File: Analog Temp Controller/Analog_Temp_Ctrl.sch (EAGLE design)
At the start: 110 parts, among them IC1 TL074D, IC3 LMV358MMX, IC4 ADA4522-2, J1 USB_MINI-B_SMT, Q1 TIP41C, T1 2N3904, T2 2N3906, U1 ADR01BRZ, U2 ATMEGA32U4-AU, U3 CJT1117-3.3-SOT223, U4 CJT1117-5.0-SOT223, U5 AD5272BRMZ-20, X1 CRYSTAL-3.2-2.5

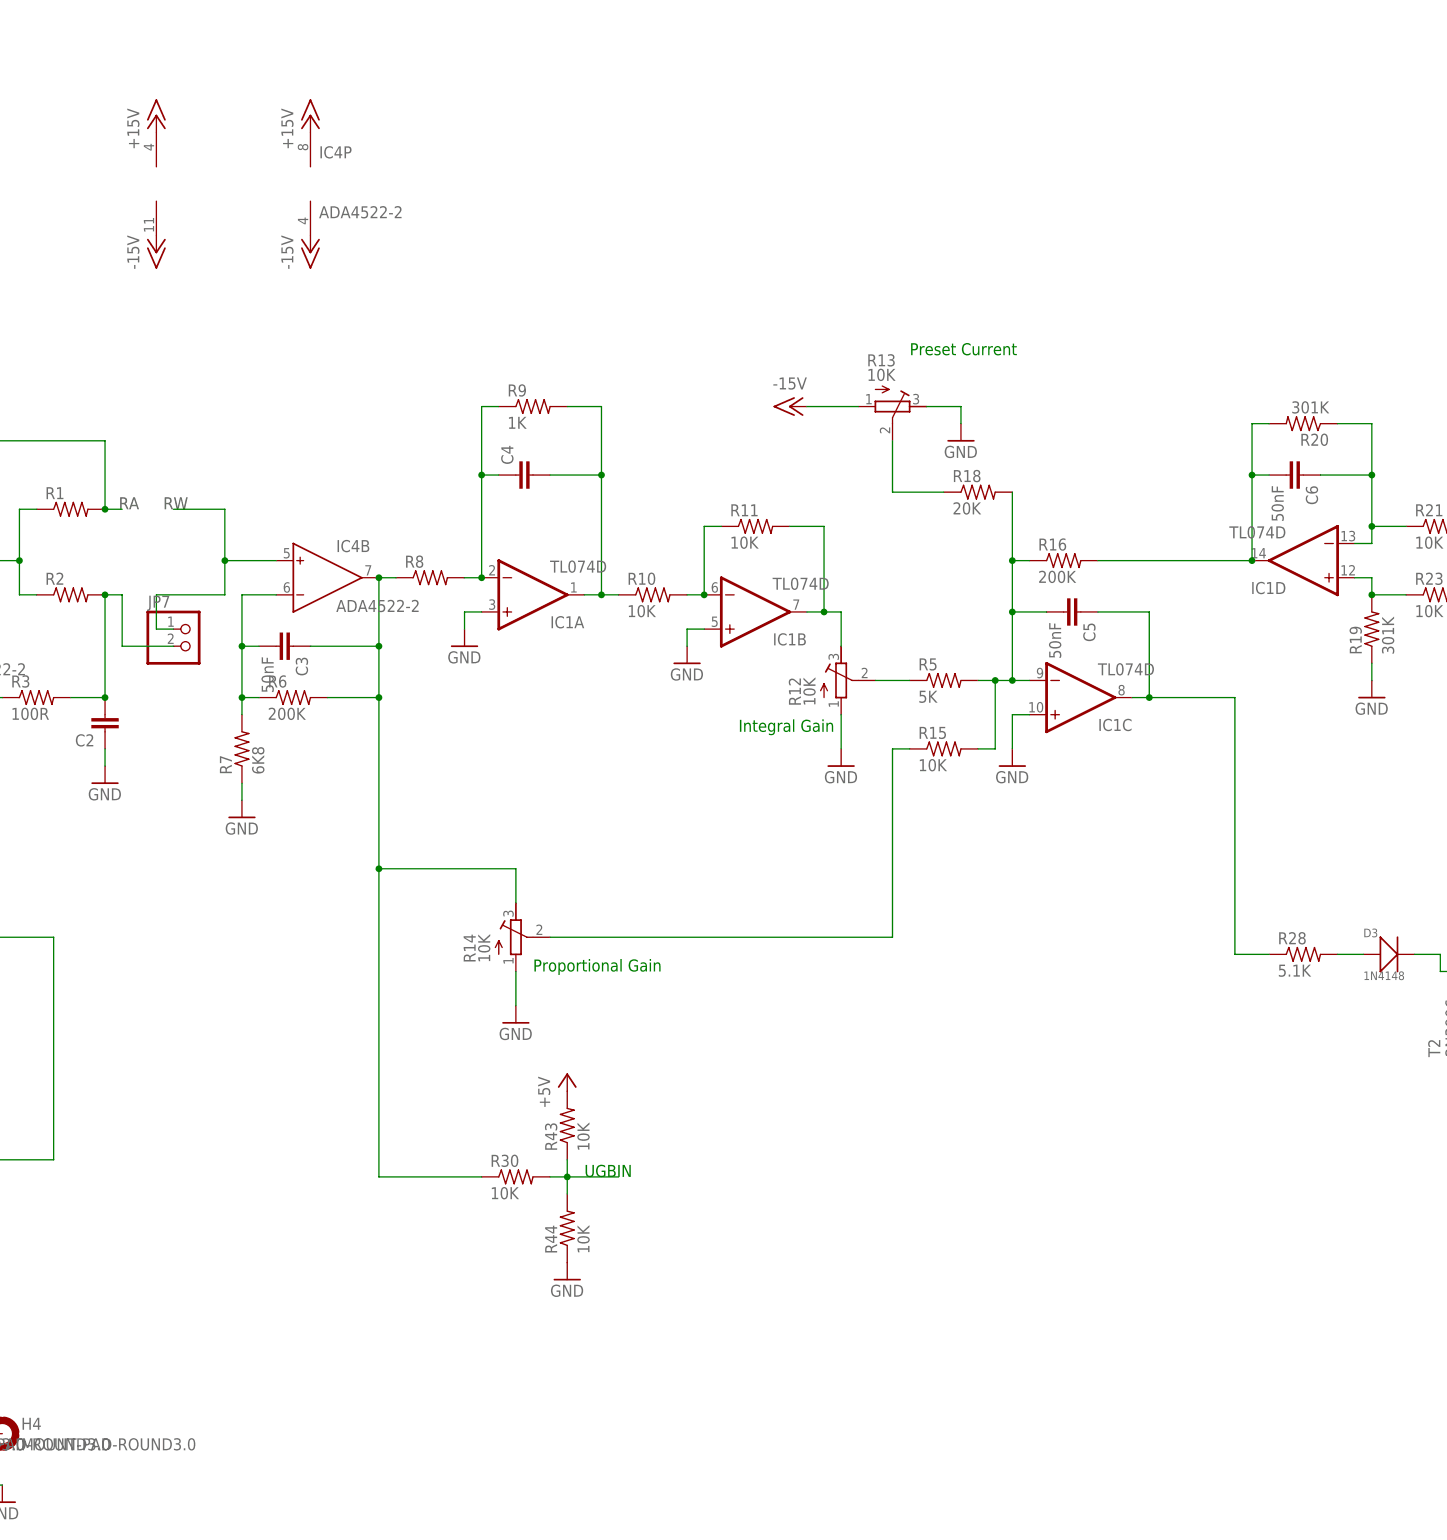
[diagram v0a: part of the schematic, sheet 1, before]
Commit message: Completed Temperature Controller, Rdy for Mfg.
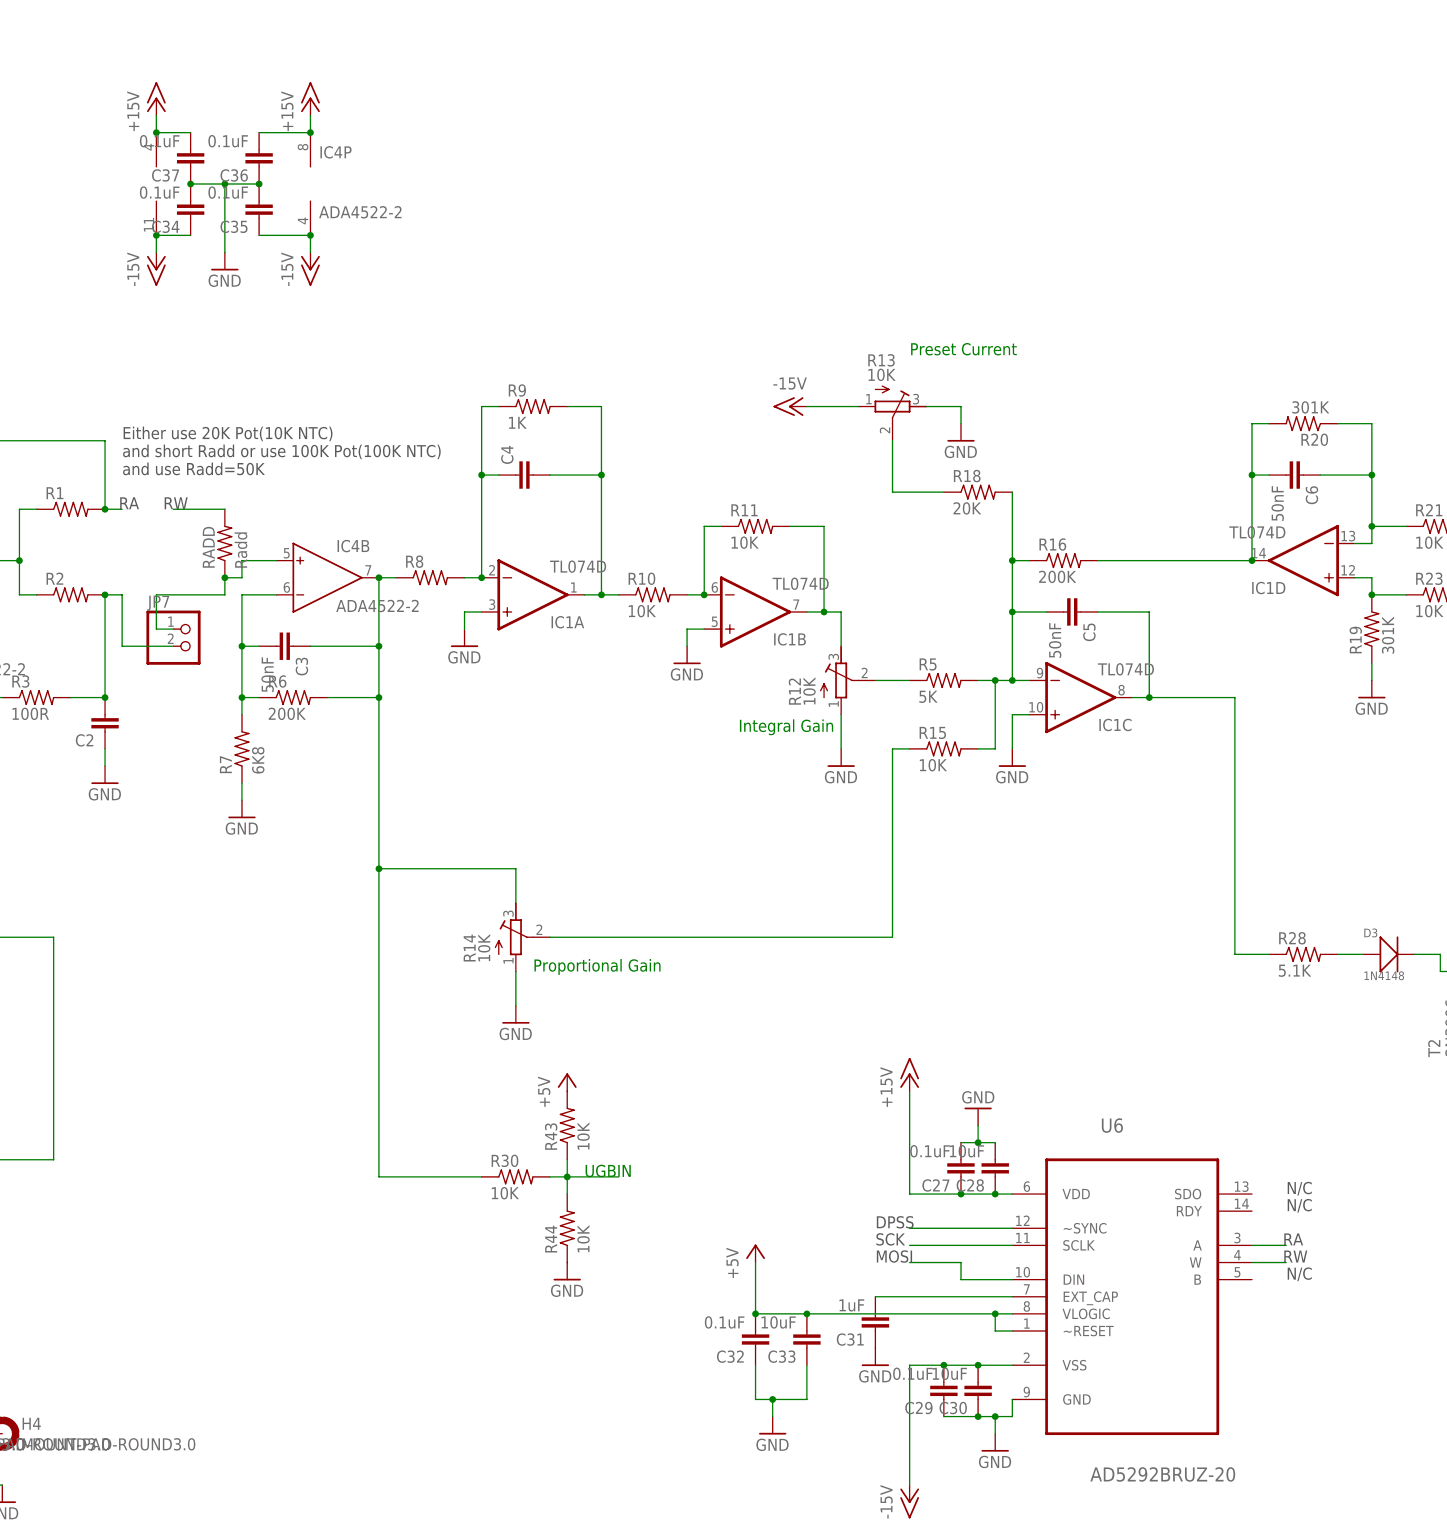
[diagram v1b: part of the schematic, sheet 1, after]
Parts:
- removed U5: AD5272BRMZ-20, Analog Devices_By_element14_Batch_1:AD5272BRMZ-20
- added C27, C29, C32, C34, C35, C36, C37: 0.1uF, rcl:C-EUC0805
- added C28, C30, C33: 10uF, rcl:C-EUC0805
- added C31: 1uF, rcl:C-EUC0805
- added RADD: Radd, rcl:R-US_R0805
- added U6: AD5292BRUZ-20, Analog Devices_By_element14_Batch_1:AD5292BRUZ-20
- renumbered LED2 to RX, LED3 to TX, LED4 to PWR
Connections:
- removed net N$52: JP8.3, U2.PF4(ADC4/TCK)
- new net DPSS: U2.PE6(INT.6/AIN0), U6.~SYNC
- new net N$39: JP8.1, U2.PF1(ADC1)
- new net N$50: C31.2, U6.EXT_CAP
- net +15V: now also C27.1, C28.1, C36.2, C37.2, U6.VDD
- net +5V: now also C32.2, C33.2, U6.VLOGIC, U6.~RESET
- net -15V: now also C29.2, C30.2, C34.1, C35.1, U6.VSS
- net GND: now also C27.2, C28.2, C29.1, C30.1, C31.1, C32.1, C33.1, C34.2, C35.2, C36.1, C37.1, U6.GND
- net MOSI: now also U6.DIN
- net N$2: now also JP8.3, U2.PF5(ADC5/TMS); no longer JP8.1, U2.PF0(ADC0)
- net N$30: now also U2.PF4(ADC4/TCK); no longer U2.PF1(ADC1)
- net N$47: now also IC4B.IN+, JP7.1, RADD.1; no longer U5.VDD, U5.~RESET
- net RA: now also U6.A; no longer U5.A
- net RW: now also RADD.2, U6.W; no longer IC4B.IN+, JP7.1, U5.W
- net SCK: now also U6.SCLK
- net UGBOUT: now also U2.PF0(ADC0); no longer U2.PF5(ADC5/TMS)
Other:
- note added: "DPSS"
- note added: "Either use 20K Pot(10K NTC) and short Radd or use 100K Pot(100K NTC) and use Radd=50K"
- note added: "N/C"
- moved on the sheet: JP8

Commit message: Preliminary changes to new version.
New features: Microntroller for current driver as well, seperate A/D
grounding, upgrade to ARM Cortec uC, several other improvements.
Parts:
- removed H1, H2, H3, H4: MOUNT-PAD-ROUND3.0, holes:MOUNT-PAD-ROUND3.0
- renumbered RADD to RA, RE to RS
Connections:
- net GND: no longer H1.MOUNT, H2.MOUNT, H3.MOUNT, H4.MOUNT
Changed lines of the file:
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@@
 <?xml version="1.0" encoding="utf-8"?>
 <!DOCTYPE eagle SYSTEM "eagle.dtd">
-<eagle version="8.4.3">
+<eagle version="8.5.0">
 <drawing>
 <settings>
@@
 <part name="GND15" library="supply1" library_urn="urn:adsk.eagle:library:371" deviceset="GND" device=""/>
 <part name="P-5" library="supply1" library_urn="urn:adsk.eagle:library:371" deviceset="-15V" device=""/>
-<part name="U1" library="Analog Devices_By_element14_Batch_1" deviceset="ADR01BRZ" device=""/>
 <part name="GND16" library="supply1" library_urn="urn:adsk.eagle:library:371" deviceset="GND" device=""/>
 <part name="P+3" library="supply1" library_urn="urn:adsk.eagle:library:371" deviceset="+15V" device=""/>
@@
 <part name="GND18" library="supply1" library_urn="urn:adsk.eagle:library:371" deviceset="GND" device=""/>
 <part name="GND19" library="supply1" library_urn="urn:adsk.eagle:library:371" deviceset="GND" device=""/>
-<part name="H1" library="holes" library_urn="urn:adsk.eagle:library:237" deviceset="MOUNT-PAD-ROUND" device="3.0" package3d_urn="urn:adsk.eagle:package:14280/1"/>
-<part name="H2" library="holes" library_urn="urn:adsk.eagle:library:237" deviceset="MOUNT-PAD-ROUND" device="3.0" package3d_urn="urn:adsk.eagle:package:14280/1"/>
-<part name="H3" library="holes" library_urn="urn:adsk.eagle:library:237" deviceset="MOUNT-PAD-ROUND" device="3.0" package3d_urn="urn:adsk.eagle:package:14280/1"/>
-<part name="H4" library="holes" library_urn="urn:adsk.eagle:library:237" deviceset="MOUNT-PAD-ROUND" device="3.0" package3d_urn="urn:adsk.eagle:package:14280/1"/>
-<part name="GND21" library="supply1" library_urn="urn:adsk.eagle:library:371" deviceset="GND" device=""/>
-<part name="GND22" library="supply1" library_urn="urn:adsk.eagle:library:371" deviceset="GND" device=""/>
-<part name="GND23" library="supply1" library_urn="urn:adsk.eagle:library:371" deviceset="GND" device=""/>
-<part name="GND24" library="supply1" library_urn="urn:adsk.eagle:library:371" deviceset="GND" device=""/>
 <part name="R12" library="rcl" library_urn="urn:adsk.eagle:library:334" deviceset="R-TRIMM" device="3296W" package3d_urn="urn:adsk.eagle:package:23739/1" value="10K"/>
 <part name="R13" library="rcl" library_urn="urn:adsk.eagle:library:334" deviceset="R-TRIMM" device="3296W" package3d_urn="urn:adsk.eagle:package:23739/1" value="10K"/>
@@
 <part name="P+4" library="supply1" library_urn="urn:adsk.eagle:library:371" deviceset="+15V" device=""/>
 <part name="P-6" library="supply1" library_urn="urn:adsk.eagle:library:371" deviceset="-15V" device=""/>
-<part name="RE" library="adafruit" library_urn="urn:adsk.eagle:library:420" deviceset="R-US_" device="R2512" value="0.5R"/>
+<part name="RS" library="adafruit" library_urn="urn:adsk.eagle:library:420" deviceset="R-US_" device="R2512" value="0.5R"/>
 <part name="U2" library="adafruit" library_urn="urn:adsk.eagle:library:420" deviceset="ATMEGA32U4" device="-AU"/>
 <part name="J1" library="SparkFun-Connectors" library_urn="urn:adsk.eagle:library:513" deviceset="USB_MINI-B" device="_SMT" package3d_urn="urn:adsk.eagle:package:38244/1"/>
@@
 <part name="C37" library="rcl" library_urn="urn:adsk.eagle:library:334" deviceset="C-EU" device="C0805" package3d_urn="urn:adsk.eagle:package:23617/2" value="0.1uF"/>
 <part name="GND53" library="supply1" library_urn="urn:adsk.eagle:library:371" deviceset="GND" device=""/>
-<part name="RADD" library="rcl" library_urn="urn:adsk.eagle:library:334" deviceset="R-US_" device="R0805" package3d_urn="urn:adsk.eagle:package:23553/2" value="Radd"/>
+<part name="RA" library="rcl" library_urn="urn:adsk.eagle:library:334" deviceset="R-US_" device="R0805" package3d_urn="urn:adsk.eagle:package:23553/2" value="Radd"/>
 <part name="P+21" library="supply1" library_urn="urn:adsk.eagle:library:371" deviceset="+5V" device=""/>
+<part name="U1" library="Analog Devices_By_element14_Batch_1" deviceset="ADR01BRZ" device=""/>
 </parts>
 <sheets>
@@
 <instance part="GND15" gate="1" x="284.48" y="177.8"/>
 <instance part="P-5" gate="1" x="264.16" y="175.26" rot="R180"/>
-<instance part="U1" gate="A" x="7.62" y="71.12"/>
 <instance part="GND16" gate="1" x="-20.32" y="48.26"/>
 <instance part="P+3" gate="1" x="-22.86" y="91.44"/>
@@
 <instance part="GND18" gate="1" x="-15.24" y="68.58"/>
 <instance part="GND19" gate="1" x="25.4" y="68.58"/>
-<instance part="H1" gate="G$1" x="5.08" y="25.4"/>
-<instance part="H2" gate="G$1" x="17.78" y="25.4"/>
-<instance part="H3" gate="G$1" x="30.48" y="25.4"/>
-<instance part="H4" gate="G$1" x="43.18" y="25.4"/>
-<instance part="GND21" gate="1" x="5.08" y="15.24"/>
-<instance part="GND22" gate="1" x="17.78" y="15.24"/>
-<instance part="GND23" gate="1" x="30.48" y="15.24"/>
-<instance part="GND24" gate="1" x="43.18" y="15.24"/>
 <instance part="R12" gate="G$1" x="167.64" y="137.16"/>
 <instance part="R13" gate="G$1" x="175.26" y="177.8" rot="R270"/>
@@
 <instance part="P+4" gate="1" x="66.04" y="223.52"/>
 <instance part="P-6" gate="1" x="66.04" y="198.12"/>
-<instance part="RE" gate="G$1" x="281.94" y="154.94" rot="R90"/>
+<instance part="RS" gate="G$1" x="281.94" y="154.94" rot="R90"/>
 <instance part="C9" gate="G$1" x="-15.24" y="73.66" rot="R180"/>
 <instance part="C10" gate="G$1" x="25.4" y="73.66" rot="R180"/>
@@
 <instance part="C37" gate="G$1" x="71.12" y="213.36" rot="R180"/>
 <instance part="GND53" gate="1" x="76.2" y="198.12"/>
-<instance part="RADD" gate="G$1" x="76.2" y="157.48" rot="R90"/>
+<instance part="RA" gate="G$1" x="76.2" y="157.48" rot="R90"/>
 <instance part="P+21" gate="1" x="154.94" y="53.34"/>
+<instance part="U1" gate="A" x="7.62" y="71.12"/>
 </instances>
 <busses>
@@
 <pinref part="GND16" gate="1" pin="GND"/>
 <wire x1="-20.32" y1="50.8" x2="-20.32" y2="55.88" width="0.1524" layer="91"/>
+<wire x1="-20.32" y1="55.88" x2="-10.16" y2="55.88" width="0.1524" layer="91"/>
 <pinref part="U1" gate="A" pin="GND"/>
-<wire x1="-20.32" y1="55.88" x2="-10.16" y2="55.88" width="0.1524" layer="91"/>
 </segment>
 <segment>
@@
 <wire x1="38.1" y1="53.34" x2="38.1" y2="50.8" width="0.1524" layer="91"/>
 <pinref part="R32" gate="G$1" pin="1"/>
-</segment>
-<segment>
-<pinref part="GND21" gate="1" pin="GND"/>
-<pinref part="H1" gate="G$1" pin="MOUNT"/>
-<wire x1="5.08" y1="17.78" x2="2.54" y2="17.78" width="0.1524" layer="91"/>
-<wire x1="2.54" y1="17.78" x2="2.54" y2="25.4" width="0.1524" layer="91"/>
-</segment>
-<segment>
-<pinref part="GND22" gate="1" pin="GND"/>
-<pinref part="H2" gate="G$1" pin="MOUNT"/>
-<wire x1="17.78" y1="17.78" x2="15.24" y2="17.78" width="0.1524" layer="91"/>
-<wire x1="15.24" y1="17.78" x2="15.24" y2="25.4" width="0.1524" layer="91"/>
-</segment>
-<segment>
-<pinref part="GND23" gate="1" pin="GND"/>
-<pinref part="H3" gate="G$1" pin="MOUNT"/>
-<wire x1="30.48" y1="17.78" x2="27.94" y2="17.78" width="0.1524" layer="91"/>
-<wire x1="27.94" y1="17.78" x2="27.94" y2="25.4" width="0.1524" layer="91"/>
-</segment>
-<segment>
-<pinref part="GND24" gate="1" pin="GND"/>
-<pinref part="H4" gate="G$1" pin="MOUNT"/>
-<wire x1="43.18" y1="17.78" x2="40.64" y2="17.78" width="0.1524" layer="91"/>
-<wire x1="40.64" y1="17.78" x2="40.64" y2="25.4" width="0.1524" layer="91"/>
 </segment>
 <segment>
@@
 <segment>
 <wire x1="76.2" y1="162.56" x2="68.58" y2="162.56" width="0.1524" layer="91"/>
-<pinref part="RADD" gate="G$1" pin="2"/>
+<pinref part="RA" gate="G$1" pin="2"/>
 </segment>
 </net>
@@
 <wire x1="281.94" y1="182.88" x2="292.1" y2="182.88" width="0.1524" layer="91"/>
 <junction x="281.94" y="182.88"/>
-<pinref part="RE" gate="G$1" pin="2"/>
+<pinref part="RS" gate="G$1" pin="2"/>
 <junction x="281.94" y="160.02"/>
 <pinref part="R22" gate="G$1" pin="2"/>
@@
 <wire x1="281.94" y1="124.46" x2="281.94" y2="129.54" width="0.1524" layer="91"/>
 <junction x="281.94" y="129.54"/>
-<pinref part="RE" gate="G$1" pin="1"/>
+<pinref part="RS" gate="G$1" pin="1"/>
 <junction x="281.94" y="149.86"/>
 <pinref part="R24" gate="G$1" pin="2"/>
@@
 <pinref part="P+3" gate="1" pin="+15V"/>
 <wire x1="-22.86" y1="88.9" x2="-22.86" y2="78.74" width="0.1524" layer="91"/>
-<pinref part="U1" gate="A" pin="VIN"/>
 <wire x1="-22.86" y1="78.74" x2="-15.24" y2="78.74" width="0.1524" layer="91"/>
 <pinref part="C9" gate="G$1" pin="2"/>
 <wire x1="-15.24" y1="78.74" x2="-10.16" y2="78.74" width="0.1524" layer="91"/>
 <junction x="-15.24" y="78.74"/>
+<pinref part="U1" gate="A" pin="VIN"/>
 </segment>
 <segment>
@@
 <net name="N$24" class="0">
 <segment>
-<pinref part="U1" gate="A" pin="VOUT"/>
 <wire x1="25.4" y1="78.74" x2="38.1" y2="78.74" width="0.1524" layer="91"/>
 <pinref part="C10" gate="G$1" pin="2"/>
+<pinref part="R31" gate="G$1" pin="2"/>
+<pinref part="U1" gate="A" pin="VOUT"/>
 <junction x="25.4" y="78.74"/>
-<pinref part="R31" gate="G$1" pin="2"/>
 </segment>
 </net>
@@
 <pinref part="JP7" gate="G$1" pin="1"/>
 <wire x1="66.04" y1="144.78" x2="68.58" y2="144.78" width="0.1524" layer="91"/>
-<pinref part="RADD" gate="G$1" pin="1"/>
+<pinref part="RA" gate="G$1" pin="1"/>
 <wire x1="76.2" y1="149.86" x2="76.2" y2="152.4" width="0.1524" layer="91"/>
 <wire x1="76.2" y1="152.4" x2="78.74" y2="152.4" width="0.1524" layer="91"/>
